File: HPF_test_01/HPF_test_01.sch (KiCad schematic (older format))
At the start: 9 parts, among them J1 BNC5-J-P-GN-RA-BH2D, J2 Conn_01x01, J3 Conn_01x01, T1 GT07-110-013, U1 SL1002A600SP

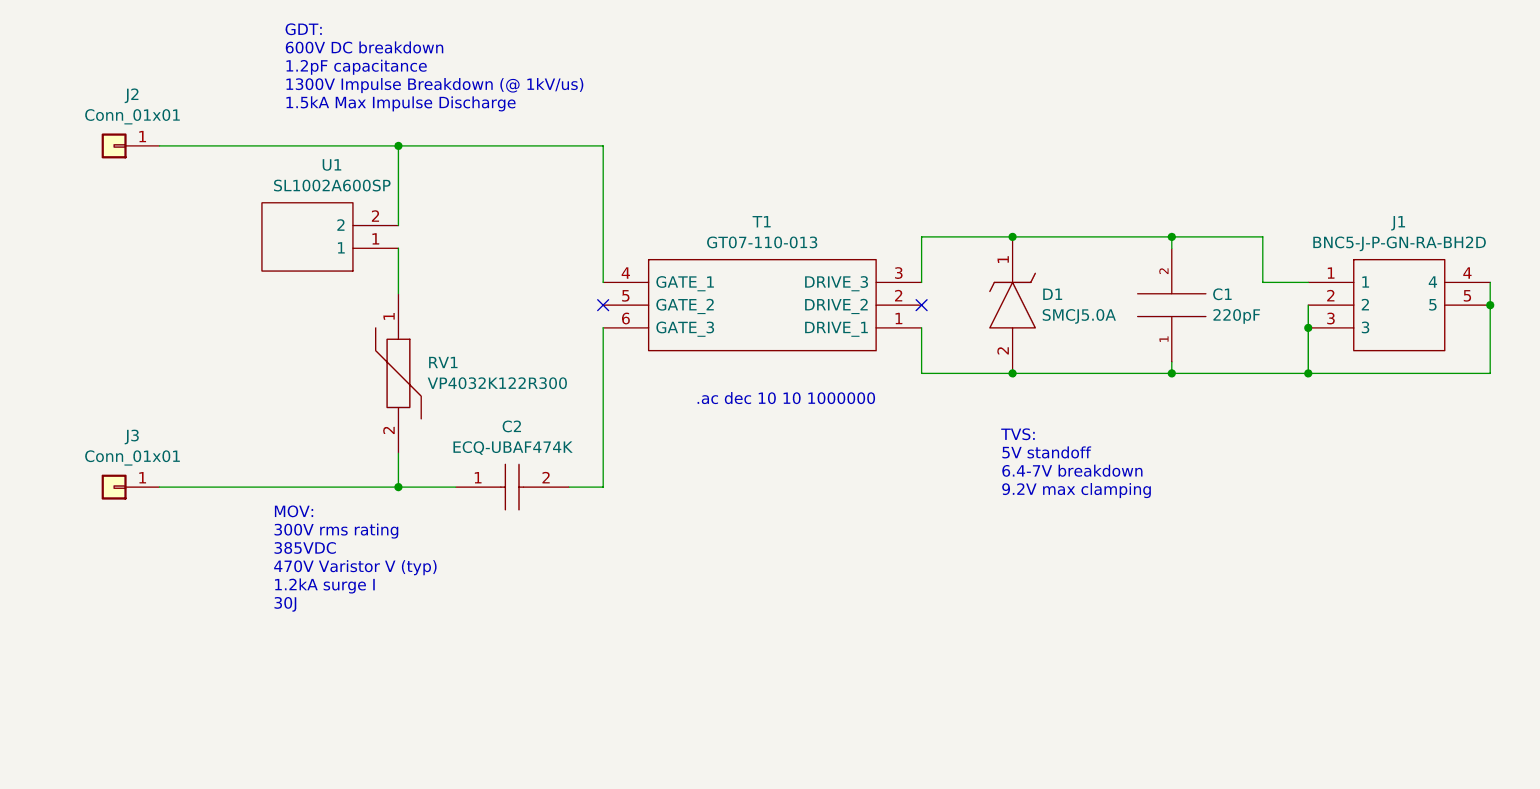
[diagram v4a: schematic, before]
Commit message: Added Banana Jack footprint
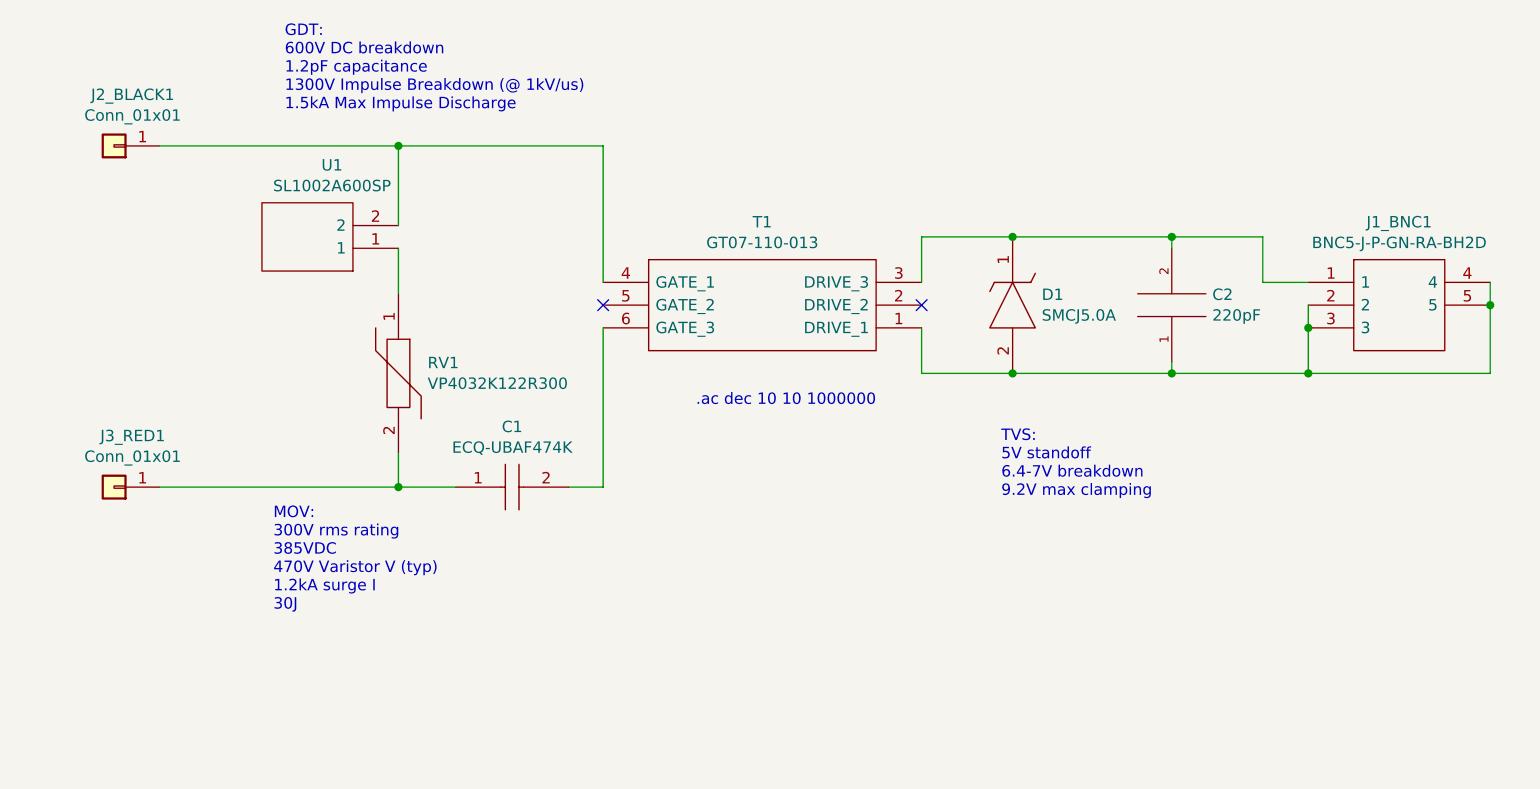
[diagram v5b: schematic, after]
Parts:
- removed T1: GT07-110-013, Kicad-GT07-models:GT07110013, symbol GT07:GT07-110-013
- added T1: GT07-110-013, GT07-110-013-Modifed:GT07110013, symbol GT07-110-013:GT07-110-013
- renumbered C2 to C1, C1 to C2, J1 to J1_BNC1, J2 to J2_BLACK1, J3 to J3_RED1
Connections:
- net at C2.1, D1.2, J1_BNC1.2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: now also T1.1 (DRIVE_1)
- net at C2.2, D1.1, J1_BNC1.1: now also T1.3 (DRIVE_3)
- net at J2_BLACK1.1 (Pin_1), U1.2: now also T1.4 (GATE_1)
- net at C1.2: now also T1.6 (GATE_3)
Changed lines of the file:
@@
 .ac dec 10 10 1000000
 $Comp
-L pspice:C C1
+L pspice:C C2
 U 1 1 619514BE
 P 7450 4300
-F 0 "C1" H 7272 4254 50  0000 R CNN
+F 0 "C2" H 7272 4254 50  0000 R CNN
 F 1 "220pF" H 7272 4345 50  0000 R CNN
 F 2 "Capacitor_SMD:C_0603_1608Metric_Pad1.05x0.95mm_HandSolder" H 7450 4300 50  0001 C CNN
@@
 	1    7450 4300
 	-1   0    0    1
-$EndComp
-$Comp
-L GT07:GT07-110-013 T1
-U 1 1 61A52B6B
-P 4950 4200
-F 0 "T1" H 5650 4465 50  0000 C CNN
-F 1 "GT07-110-013" H 5650 4374 50  0000 C CNN
-F 2 "Kicad-GT07-models:GT07110013" H 6200 4300 50  0001 L CNN
-F 3 "https://componentsearchengine.com/Datasheets/1/GT07-110-013.pdf" H 6200 4200 50  0001 L CNN
-F 4 "Pulse Transformers" H 6200 4100 50  0001 L CNN "Description"
-F 5 "6.35" H 6200 4000 50  0001 L CNN "Height"
-F 6 "911-GT07-110-013" H 6200 3900 50  0001 L CNN "Mouser Part Number"
-F 7 "https://www.mouser.co.uk/ProductDetail/ICE-Components/GT07-110-013?qs=UkDUCjYnTB00rEvMCOsFKQ%3D%3D" H 6200 3800 50  0001 L CNN "Mouser Price/Stock"
-F 8 "ICE Components" H 6200 3700 50  0001 L CNN "Manufacturer_Name"
-F 9 "GT07-110-013" H 6200 3600 50  0001 L CNN "Manufacturer_Part_Number"
-F 10 "X" H 4950 4200 50  0001 C CNN "Spice_Primitive"
-F 11 "gt07-110-013" H 4950 4200 50  0001 C CNN "Spice_Model"
-F 12 "Y" H 4950 4200 50  0001 C CNN "Spice_Netlist_Enabled"
-F 13 "/Users/MacMini/Documents/KiCad/HPF/Kicad-GT07-models/GT07-110-013.lib" H 4950 4200 50  0001 C CNN "Spice_Lib_File"
-	1    4950 4200
-	1    0    0    -1
 $EndComp
 NoConn ~ 6350 4300
@@
 $EndComp
 $Comp
-L BNC5-J-P-GN-RA-BH2D:BNC5-J-P-GN-RA-BH2D J1
+L BNC5-J-P-GN-RA-BH2D:BNC5-J-P-GN-RA-BH2D J1_BNC1
 U 1 1 61CAB142
 P 8050 4200
-F 0 "J1" H 8450 4465 50  0000 C CNN
+F 0 "J1_BNC1" H 8450 4465 50  0000 C CNN
 F 1 "BNC5-J-P-GN-RA-BH2D" H 8450 4374 50  0000 C CNN
 F 2 "BNC5-J-P-GN-RA-BH2D_kicad:BNC5JPGNRABH2D" H 8700 4300 50  0001 L CNN
@@
 $EndComp
 $Comp
-L ECQ-UBAF474K:ECQ-UBAF474K C2
+L ECQ-UBAF474K:ECQ-UBAF474K C1
 U 1 1 61CAD9E9
 P 4300 5100
-F 0 "C2" H 4550 5365 50  0000 C CNN
+F 0 "C1" H 4550 5365 50  0000 C CNN
 F 1 "ECQ-UBAF474K" H 4550 5274 50  0000 C CNN
 F 2 "ECQUBAF474K" H 4650 5150 50  0001 L CNN
@@
 Connection ~ 8850 4300
 $Comp
-L Connector_Generic:Conn_01x01 J2
+L Connector_Generic:Conn_01x01 J2_BLACK1
 U 1 1 61CBC9A8
 P 2800 3600
-F 0 "J2" H 2718 3375 50  0000 C CNN
+F 0 "J2_BLACK1" H 2718 3375 50  0000 C CNN
 F 1 "Conn_01x01" H 2718 3466 50  0000 C CNN
 F 2 "Connector_Coaxial:SMA_Amphenol_132203-12_Horizontal" H 2800 3600 50  0001 C CNN
@@
 $EndComp
 $Comp
-L Connector_Generic:Conn_01x01 J3
+L Connector_Generic:Conn_01x01 J3_RED1
 U 1 1 61CBCE04
 P 2800 5100
-F 0 "J3" H 2718 4875 50  0000 C CNN
+F 0 "J3_RED1" H 2718 4875 50  0000 C CNN
 F 1 "Conn_01x01" H 2718 4966 50  0000 C CNN
 F 2 "Connector_Coaxial:SMA_Amphenol_132203-12_Horizontal" H 2800 5100 50  0001 C CNN
@@
 	-1   0    0    1
 $EndComp
+$Comp
+L GT07-110-013:GT07-110-013 T1
+U 1 1 61D390B4
+P 4950 4200
+F 0 "T1" H 5650 4465 50  0000 C CNN
+F 1 "GT07-110-013" H 5650 4374 50  0000 C CNN
+F 2 "GT07-110-013-Modifed:GT07110013" H 6200 4300 50  0001 L CNN
+F 3 "https://componentsearchengine.com/Datasheets/1/GT07-110-013.pdf" H 6200 4200 50  0001 L CNN
+F 4 "Pulse Transformers" H 6200 4100 50  0001 L CNN "Description"
+F 5 "6.35" H 6200 4000 50  0001 L CNN "Height"
+F 6 "911-GT07-110-013" H 6200 3900 50  0001 L CNN "Mouser Part Number"
+F 7 "https://www.mouser.co.uk/ProductDetail/ICE-Components/GT07-110-013?qs=UkDUCjYnTB00rEvMCOsFKQ%3D%3D" H 6200 3800 50  0001 L CNN "Mouser Price/Stock"
+F 8 "ICE Components" H 6200 3700 50  0001 L CNN "Manufacturer_Name"
+F 9 "GT07-110-013" H 6200 3600 50  0001 L CNN "Manufacturer_Part_Number"
+	1    4950 4200
+	1    0    0    -1
+$EndComp
 $EndSCHEMATC

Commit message: PCB: Added traces, edgecuts, & accurate bananajack footprint. SPICE: Added spice data folders & updated eeschema simulation. 3D: Added 3d render folder and initial board render
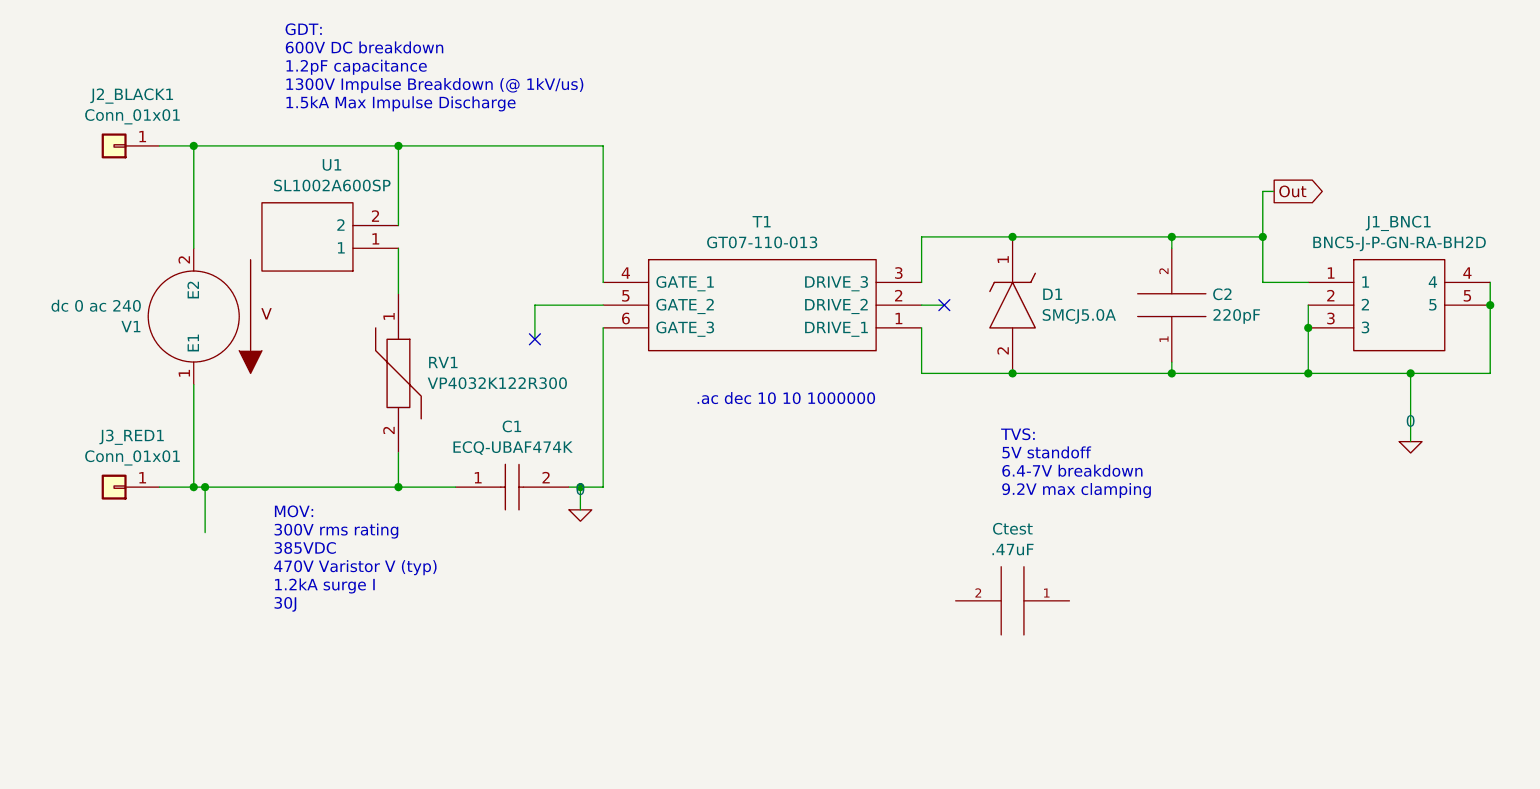
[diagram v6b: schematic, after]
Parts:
- added Ctest: .47uF, symbol pspice:C
- added V1: dc 0 ac 240, symbol pspice:VSOURCE
- C1: Spice_Model (none) -> 0.47uF; Spice_Netlist_Enabled (none) -> Y; Spice_Primitive (none) -> C
- D1: Spice_Lib_File (none) -> /Users/MacMini/Documents/KiCad/HPF/HPF_SPICE/SMCJ5.0A_spice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; Spice_Model (none) -> SMCJ; Spice_Netlist_Enabled (none) -> Y; Spice_Primitive (none) -> X
- J1_BNC1, J2_BLACK1, J3_RED1: Spice_Model (none) -> 1; Spice_Netlist_Enabled (none) -> N; Spice_Primitive (none) -> R
- RV1, U1: Spice_Model (none) -> 1meg; Spice_Netlist_Enabled (none) -> Y; Spice_Primitive (none) -> R
- T1: Spice_Lib_File (none) -> /Users/MacMini/Documents/KiCad/HPF/HPF_SPICE/GTRANS_01.lib; Spice_Model (none) -> GTRANS; Spice_Netlist_Enabled (none) -> Y; Spice_Primitive (none) -> X
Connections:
- net 0: now reaches C2.1, D1.2, J1_BNC1.2, J1_BNC1.3, J1_BNC1.4, J1_BNC1.5, T1.1 (DRIVE_1)
- net 0: now also C1.2, T1.6 (GATE_3)
- net Out: now reaches C2.2, D1.1, J1_BNC1.1, T1.3 (DRIVE_3)
- net at C1.1, J3_RED1.1 (Pin_1), RV1.2: now also V1.1 (E1)
- net at J2_BLACK1.1 (Pin_1), T1.4 (GATE_1), U1.2: now also V1.2 (E2)
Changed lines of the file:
@@
 	-1   0    0    1
 $EndComp
-NoConn ~ 6350 4300
-NoConn ~ 4950 4300
 Wire Wire Line
 	4950 3600 4950 4200
 Wire Wire Line
-	4950 5100 4800 5100
+	4950 5100 4850 5100
 Wire Wire Line
 	4950 4400 4950 5100
@@
 F 8 "Kemet" H 4600 3700 50  0001 L CNN "Manufacturer_Name"
 F 9 "VP4032K122R300" H 4600 3600 50  0001 L CNN "Manufacturer_Part_Number"
+F 10 "R" H 4050 4250 50  0001 C CNN "Spice_Primitive"
+F 11 "1meg" H 4050 4250 50  0001 C CNN "Spice_Model"
+F 12 "Y" H 4050 4250 50  0001 C CNN "Spice_Netlist_Enabled"
 	1    4050 4250
 	0    1    1    0
@@
 F 8 "LITTELFUSE" H 4700 3550 50  0001 L CNN "Manufacturer_Name"
 F 9 "SL1002A600SP" H 4700 3450 50  0001 L CNN "Manufacturer_Part_Number"
+F 10 "R" H 4050 4050 50  0001 C CNN "Spice_Primitive"
+F 11 "1meg" H 4050 4050 50  0001 C CNN "Spice_Model"
+F 12 "Y" H 4050 4050 50  0001 C CNN "Spice_Netlist_Enabled"
 	1    4050 4050
 	-1   0    0    1
 $EndComp
 Wire Wire Line
-	3000 3600 4050 3600
-Wire Wire Line
-	3000 5100 4050 5100
+	3000 3600 3150 3600
+Wire Wire Line
+	3000 5100 3150 5100
 Wire Wire Line
 	4050 4250 4050 4050
@@
 F 8 "LITTELFUSE" H 7150 3550 50  0001 L BNN "Manufacturer_Name"
 F 9 "SMCJ5.0A" H 7150 3450 50  0001 L BNN "Manufacturer_Part_Number"
+F 10 "X" H 6750 4000 50  0001 C CNN "Spice_Primitive"
+F 11 "SMCJ" H 6750 4000 50  0001 C CNN "Spice_Model"
+F 12 "Y" H 6750 4000 50  0001 C CNN "Spice_Netlist_Enabled"
+F 13 "/Users/MacMini/Documents/KiCad/HPF/HPF_SPICE/SMCJ5.0A_spice.lib" H 6750 4000 50  0001 C CNN "Spice_Lib_File"
 	1    6750 4000
 	0    1    1    0
@@
 F 8 "SAMTEC" H 8700 3700 50  0001 L CNN "Manufacturer_Name"
 F 9 "BNC5-J-P-GN-RA-BH2D" H 8700 3600 50  0001 L CNN "Manufacturer_Part_Number"
+F 10 "R" H 8050 4200 50  0001 C CNN "Spice_Primitive"
+F 11 "1" H 8050 4200 50  0001 C CNN "Spice_Model"
+F 12 "N" H 8050 4200 50  0001 C CNN "Spice_Netlist_Enabled"
 	1    8050 4200
 	1    0    0    -1
@@
 F 8 "Panasonic" H 4650 4550 50  0001 L CNN "Manufacturer_Name"
 F 9 "ECQ-UBAF474K" H 4650 4450 50  0001 L CNN "Manufacturer_Part_Number"
+F 10 "C" H 4300 5100 50  0001 C CNN "Spice_Primitive"
+F 11 "0.47uF" H 4300 5100 50  0001 C CNN "Spice_Model"
+F 12 "Y" H 4300 5100 50  0001 C CNN "Spice_Netlist_Enabled"
 	1    4300 5100
 	1    0    0    -1
@@
 	8850 4300 8850 4600
 Wire Wire Line
-	8850 4600 8050 4600
+	8850 4600 8500 4600
 Connection ~ 8050 4600
 Wire Wire Line
@@
 F 2 "Connector_Coaxial:SMA_Amphenol_132203-12_Horizontal" H 2800 3600 50  0001 C CNN
 F 3 "~" H 2800 3600 50  0001 C CNN
+F 4 "R" H 2800 3600 50  0001 C CNN "Spice_Primitive"
+F 5 "1" H 2800 3600 50  0001 C CNN "Spice_Model"
+F 6 "N" H 2800 3600 50  0001 C CNN "Spice_Netlist_Enabled"
 	1    2800 3600
 	-1   0    0    1
@@
 F 2 "Connector_Coaxial:SMA_Amphenol_132203-12_Horizontal" H 2800 5100 50  0001 C CNN
 F 3 "~" H 2800 5100 50  0001 C CNN
+F 4 "R" H 2800 5100 50  0001 C CNN "Spice_Primitive"
+F 5 "1" H 2800 5100 50  0001 C CNN "Spice_Model"
+F 6 "N" H 2800 5100 50  0001 C CNN "Spice_Netlist_Enabled"
 	1    2800 5100
 	-1   0    0    1
@@
 F 8 "ICE Components" H 6200 3700 50  0001 L CNN "Manufacturer_Name"
 F 9 "GT07-110-013" H 6200 3600 50  0001 L CNN "Manufacturer_Part_Number"
+F 10 "X" H 4950 4200 50  0001 C CNN "Spice_Primitive"
+F 11 "GTRANS" H 4950 4200 50  0001 C CNN "Spice_Model"
+F 12 "Y" H 4950 4200 50  0001 C CNN "Spice_Netlist_Enabled"
+F 13 "/Users/MacMini/Documents/KiCad/HPF/HPF_SPICE/GTRANS_01.lib" H 4950 4200 50  0001 C CNN "Spice_Lib_File"
 	1    4950 4200
 	1    0    0    -1
 $EndComp
+$Comp
+L pspice:0 #GND?
+U 1 1 61D5C253
+P 8500 4900
+F 0 "#GND?" H 8500 4800 50  0001 C CNN
+F 1 "0" H 8500 4989 50  0000 C CNN
+F 2 "" H 8500 4900 50  0001 C CNN
+F 3 "~" H 8500 4900 50  0001 C CNN
+	1    8500 4900
+	1    0    0    -1
+$EndComp
+$Comp
+L pspice:VSOURCE V1
+U 1 1 61D5C742
+P 3150 4350
+F 0 "V1" H 3378 4396 50  0000 L CNN
+F 1 "dc 0 ac 240" H 3378 4305 50  0000 L CNN
+F 2 "" H 3150 4350 50  0001 C CNN
+F 3 "~" H 3150 4350 50  0001 C CNN
+	1    3150 4350
+	-1   0    0    1
+$EndComp
+Wire Wire Line
+	3200 5300 3200 5100
+Connection ~ 3200 5100
+Wire Wire Line
+	3200 5100 4050 5100
+Wire Wire Line
+	3150 4650 3150 5100
+Connection ~ 3150 5100
+Wire Wire Line
+	3150 5100 3200 5100
+Wire Wire Line
+	3150 4050 3150 3600
+Connection ~ 3150 3600
+Wire Wire Line
+	3150 3600 4050 3600
+Wire Wire Line
+	8500 4900 8500 4600
+Connection ~ 8500 4600
+Wire Wire Line
+	8500 4600 8050 4600
+Text GLabel 7900 3800 2    50   Output ~ 0
+Out
+Wire Wire Line
+	7900 3800 7850 3800
+Wire Wire Line
+	7850 3800 7850 4000
+Connection ~ 7850 4000
+$Comp
+L pspice:C Ctest
+U 1 1 61D7329D
+P 6750 5600
+F 0 "Ctest" V 6435 5600 50  0000 C CNN
+F 1 ".47uF" V 6526 5600 50  0000 C CNN
+F 2 "" H 6750 5600 50  0001 C CNN
+F 3 "~" H 6750 5600 50  0001 C CNN
+F 4 "C" H 6750 5600 50  0001 C CNN "Spice_Primitive"
+F 5 ".47u" H 6750 5600 50  0001 C CNN "Spice_Model"
+F 6 "N" H 6750 5600 50  0001 C CNN "Spice_Netlist_Enabled"
+	1    6750 5600
+	0    1    1    0
+$EndComp
+$Comp
+L pspice:0 #GND?
+U 1 1 61D77CD5
+P 4850 5200
+F 0 "#GND?" H 4850 5100 50  0001 C CNN
+F 1 "0" H 4850 5289 50  0000 C CNN
+F 2 "" H 4850 5200 50  0001 C CNN
+F 3 "~" H 4850 5200 50  0001 C CNN
+	1    4850 5200
+	1    0    0    -1
+$EndComp
+Wire Wire Line
+	4950 4300 4650 4300
+Wire Wire Line
+	4650 4300 4650 4450
+Wire Wire Line
+	6450 4300 6350 4300
+Wire Wire Line
+	4850 5200 4850 5100
+Connection ~ 4850 5100
+Wire Wire Line
+	4850 5100 4800 5100
+NoConn ~ 6450 4300
+NoConn ~ 4650 4450
 $EndSCHEMATC
